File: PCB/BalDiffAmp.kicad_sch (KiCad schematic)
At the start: 15 parts, among them U5 TPA6120A2

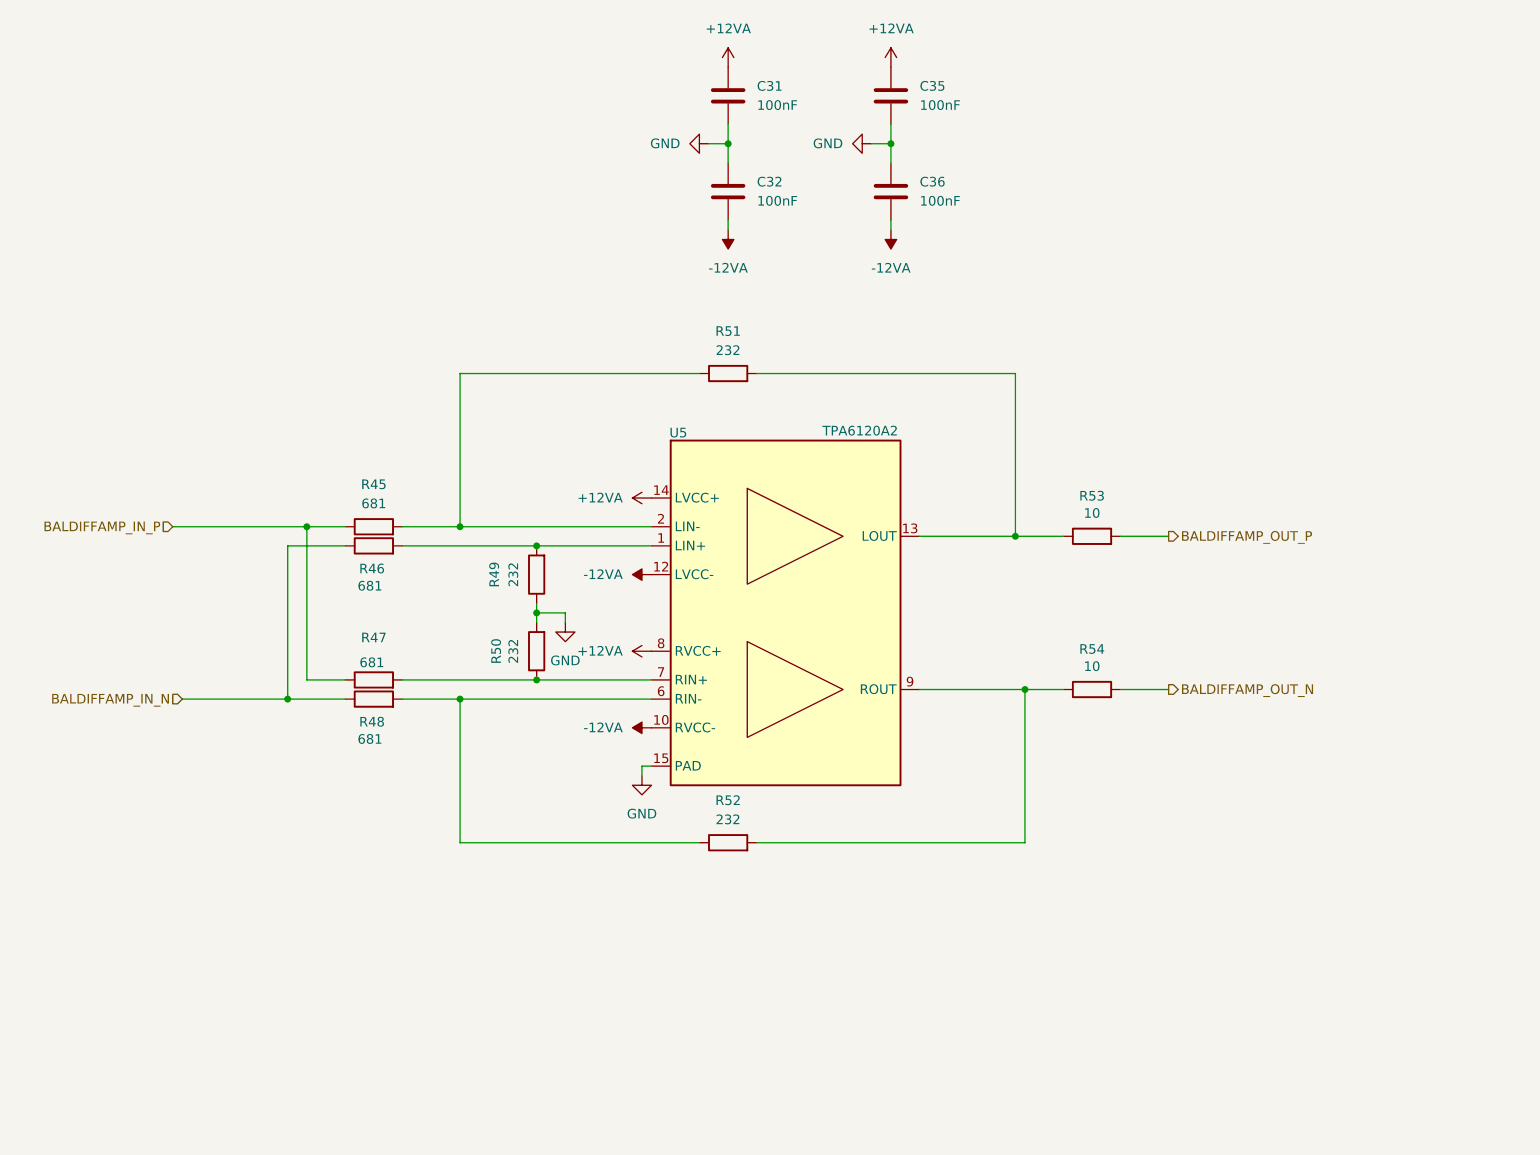
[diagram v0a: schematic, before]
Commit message: Added power supply and adjusted the AMP section to use only OPA1622 as output amp. In sync with Live 16
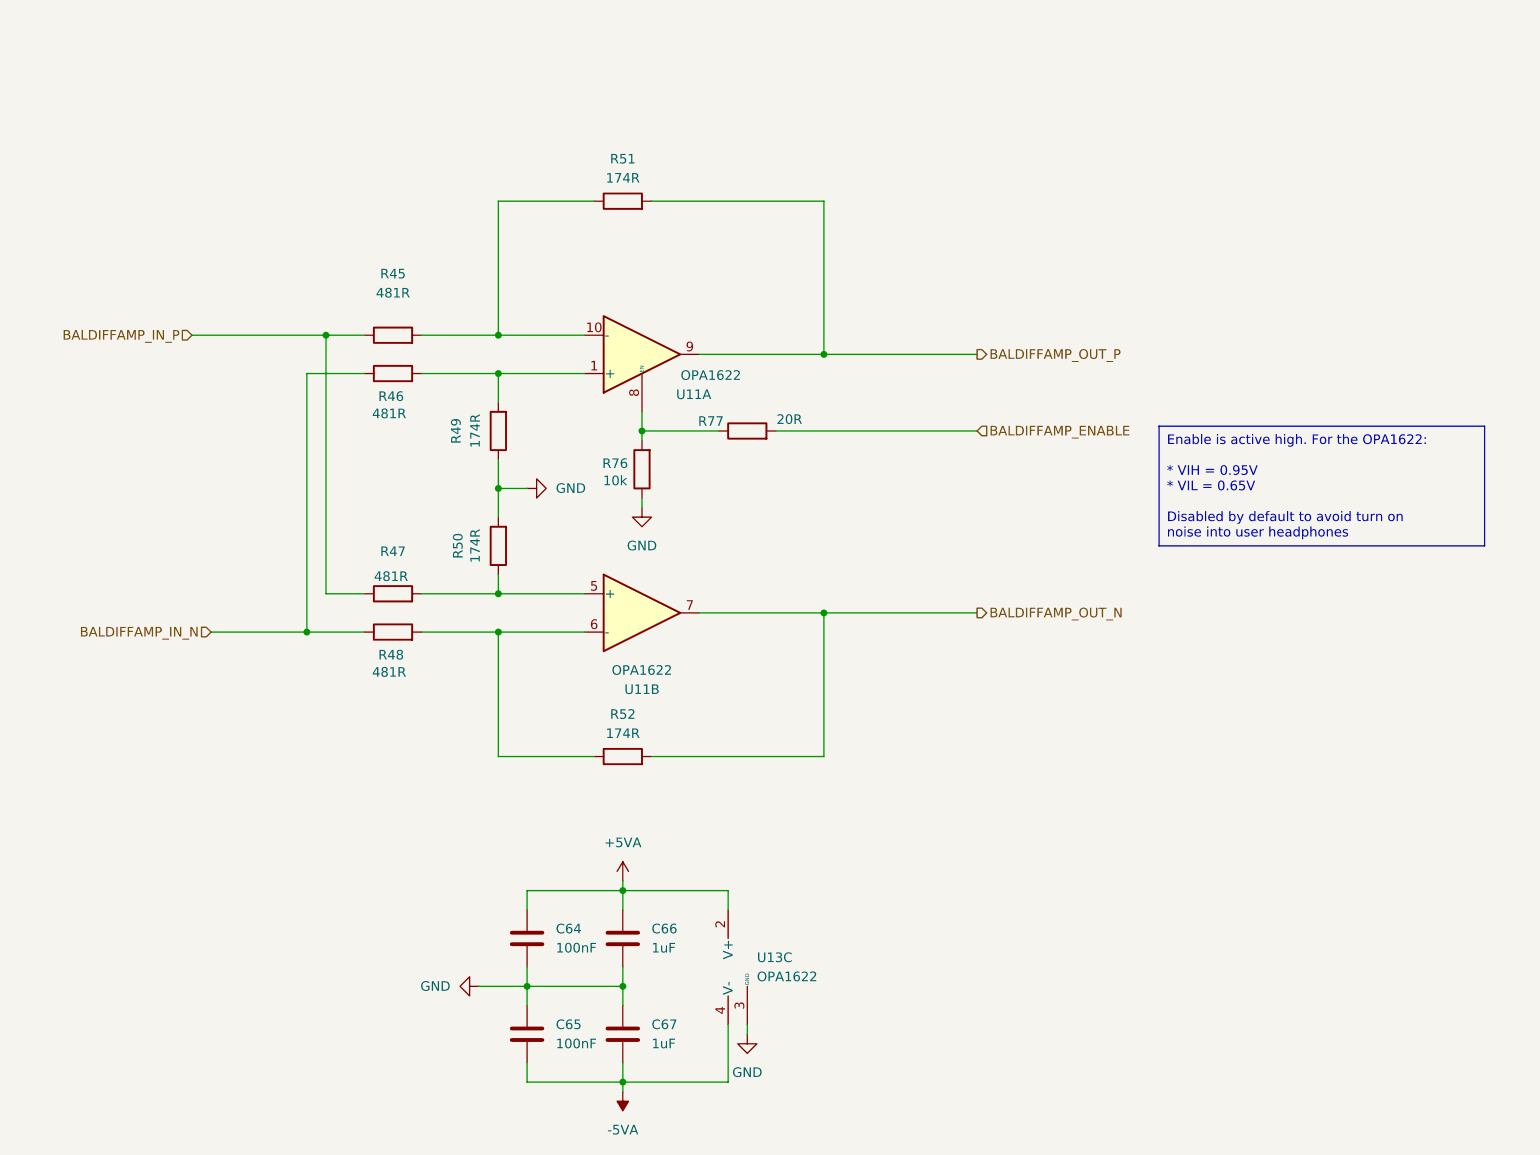
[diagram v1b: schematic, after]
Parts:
- removed C31, C32, C35, C36: 100nF, Capacitor_SMD:C_0402_1005Metric_Pad0.74x0.62mm_HandSolder, symbol Device:C
- removed R53, R54: 10, Resistor_SMD:R_0402_1005Metric_Pad0.72x0.64mm_HandSolder, symbol Device:R
- removed U5: TPA6120A2, _mahaudio KiCad Library:QFN-14_EP_3.5x3.5_Pitch0.5mm, symbol mahaudio_kicad_lib:TPA6120A2RGY
- added C64, C65: 100nF, Capacitor_SMD:C_0402_1005Metric_Pad0.74x0.62mm_HandSolder, symbol Device:C
- added C66, C67: 1uF, Capacitor_SMD:C_0402_1005Metric_Pad0.74x0.62mm_HandSolder, symbol Device:C
- added R76: 10k, Resistor_SMD:R_0402_1005Metric_Pad0.72x0.64mm_HandSolder, symbol Device:R
- added R77: 20R, Resistor_SMD:R_0402_1005Metric_Pad0.72x0.64mm_HandSolder, symbol Device:R
- added U11, U13: OPA1622, Package_SON:Texas_S-PVSON-N10, symbol Amplifier_Audio:OPA1622
- R45, R46, R47, R48: value 681 -> 481R; Tolerance (none) -> 0.1%
- R49, R50, R51, R52: value 232 -> 174R; Tolerance (none) -> 0.1%
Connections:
- net BALDIFFAMP_OUT_N: now also R52.2, U11.7
- net BALDIFFAMP_OUT_P: now also R51.2, U11.9
- net GND: now also C64.2, C65.1, C66.2, C67.1, R76.1, U13.3 (GND)
- net at R45.2, R51.1: now also U11.10 (-)
- net at R46.2, R49.2: now also U11.1 (+)
- net at R48.2, R52.1: now also U11.6 (-)
- net at R47.2, R50.1: now also U11.5 (+)
- new net: R76.2, R77.1, U11.8 (EN)
- new net +5VA: C64.1, C66.1, U13.2 (V+)
- new net -5VA: C65.2, C67.2, U13.11 (V-), U13.4 (V-)
- new net BALDIFFAMP_ENABLE: R77.2
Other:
- moved on the sheet: R45, R46, R47, R48, R49, R50, R51, R52

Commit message: Added E2P and testpoints
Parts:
- C66, C67: footprint Capacitor_SMD:C_0402_1005Metric_Pad0.74x0.62mm_HandSolder -> Capacitor_SMD:C_0603_1608Metric_Pad1.08x0.95mm_HandSolder
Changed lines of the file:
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@@
 			)
 		)
-		(property "Footprint" "Capacitor_SMD:C_0402_1005Metric_Pad0.74x0.62mm_HandSolder"
+		(property "Footprint" "Capacitor_SMD:C_0603_1608Metric_Pad1.08x0.95mm_HandSolder"
 			(at 140.6652 153.67 0)
 			(effects
@@
 			)
 		)
-		(property "Footprint" "Capacitor_SMD:C_0402_1005Metric_Pad0.74x0.62mm_HandSolder"
+		(property "Footprint" "Capacitor_SMD:C_0603_1608Metric_Pad1.08x0.95mm_HandSolder"
 			(at 140.6652 166.37 0)
 			(effects

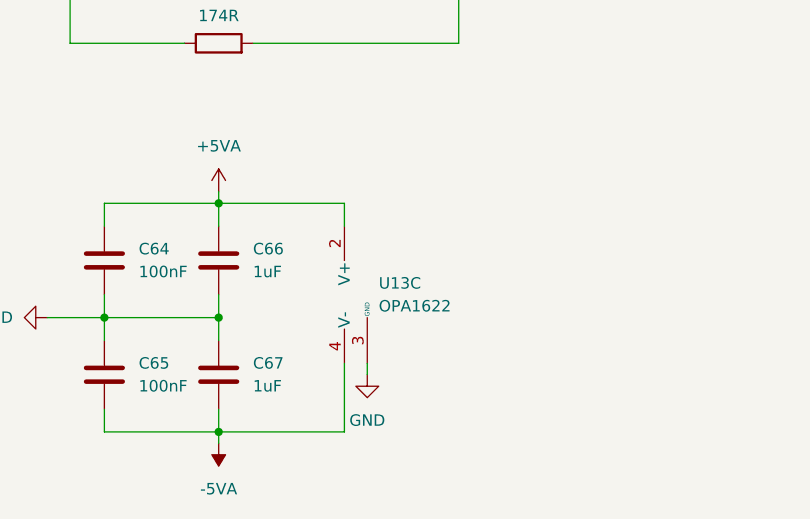
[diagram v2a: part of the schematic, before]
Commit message: Finished basic placement
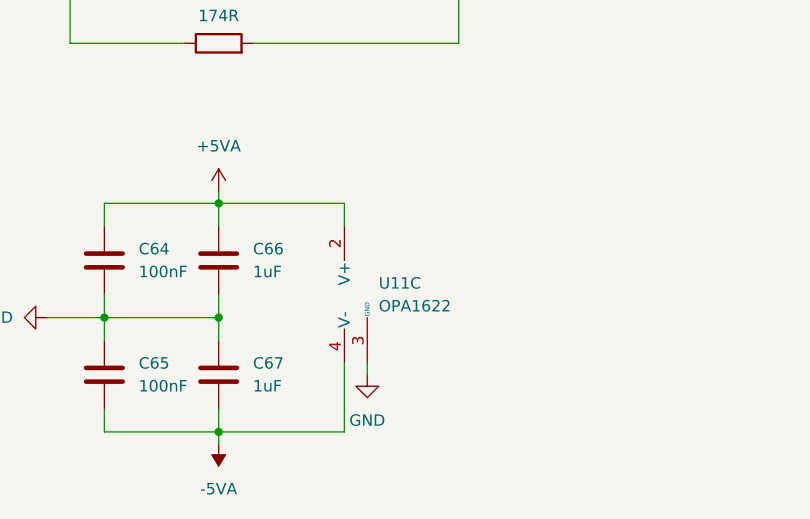
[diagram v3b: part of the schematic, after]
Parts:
- renumbered U13 to U11
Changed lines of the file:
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@@
 		(dnp no)
 		(fields_autoplaced yes)
-		(property "Reference" "U13"
+		(property "Reference" "U11"
 			(at 157.48 152.3999 0)
 			(effects
@@
 			(project "mhd314"
 				(path "/afee45fc-2361-4efb-9cde-757fc2efd57b/913309c3-489c-42b3-afc6-179d92cffcea/1a7c2388-0e9a-4978-b565-aab0f7919656"
-					(reference "U13")
+					(reference "U11")
 					(unit 3)
 				)
 				(path "/afee45fc-2361-4efb-9cde-757fc2efd57b/913309c3-489c-42b3-afc6-179d92cffcea/9f9c7045-f919-4646-b118-b603b053c849"
-					(reference "U12")
+					(reference "U4")
 					(unit 3)
 				)

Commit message: Routing revised, added some missing parameters to components
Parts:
- C66, C67: Voltage 6.3V -> 16V
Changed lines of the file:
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@@
 			)
 		)
-		(property "Voltage" "6.3V"
+		(property "Voltage" "16V"
 			(at 139.7 149.86 0)
 			(effects
@@
 			)
 		)
-		(property "Voltage" "6.3V"
+		(property "Voltage" "16V"
 			(at 139.7 162.56 0)
 			(effects

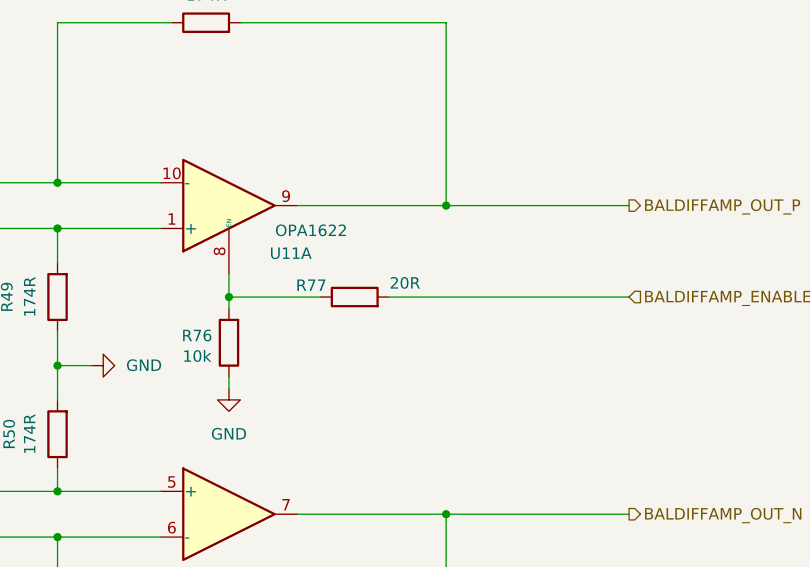
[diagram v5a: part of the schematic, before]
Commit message: Updated PCB with digital traxce suggestions. Added JLCPCB Pns
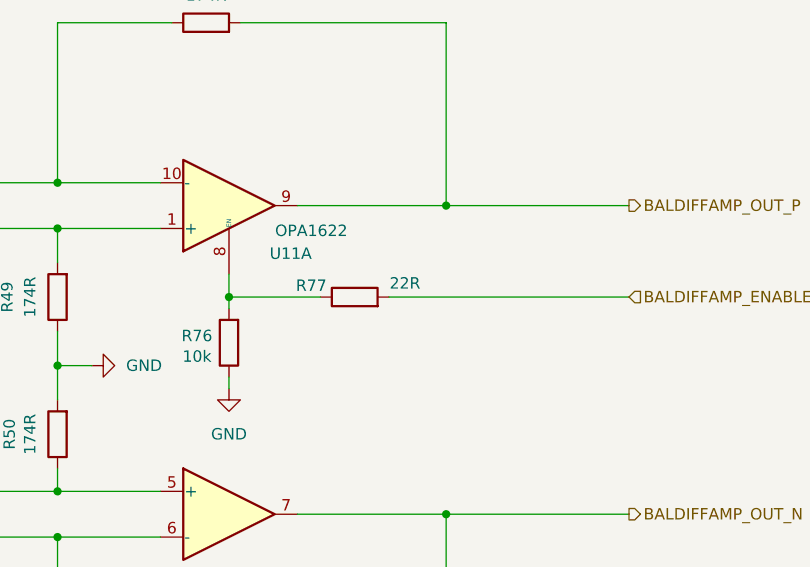
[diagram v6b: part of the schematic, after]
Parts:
- C64, C65: JLCPCBPn (none) -> C1525; Voltage 25V -> 16V
- C66, C67: JLCPCBPn (none) -> C15849
- R76: JLCPCBPn (none) -> C25744
- R77: value 20R -> 22R; JLCPCBPn (none) -> C25092
- U11: JLCPCBPn (none) -> C2876559
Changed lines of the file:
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@@
 			)
 		)
-		(property "Voltage" "25V"
+		(property "Voltage" "16V"
+			(at 127 149.86 0)
+			(effects
+				(font
+					(size 1.27 1.27)
+				)
+				(hide yes)
+			)
+		)
+		(property "JLCPCBPn" "C1525"
 			(at 127 149.86 0)
 			(effects
@@
 			)
 		)
+		(property "JLCPCBPn" "C2876559"
+			(at 142.24 106.68 0)
+			(effects
+				(font
+					(size 1.27 1.27)
+				)
+				(hide yes)
+			)
+		)
 		(pin "4"
 		)
@@
 			)
 		)
+		(property "JLCPCBPn" "C15849"
+			(at 139.7 149.86 0)
+			(effects
+				(font
+					(size 1.27 1.27)
+				)
+				(hide yes)
+			)
+		)
 		(pin "1"
 		)
@@
 			)
 		)
+		(property "JLCPCBPn" "C2876559"
+			(at 156.21 153.67 0)
+			(effects
+				(font
+					(size 1.27 1.27)
+				)
+				(hide yes)
+			)
+		)
 		(pin "4"
 		)
@@
 			)
 		)
-		(property "Voltage" "25V"
+		(property "Voltage" "16V"
+			(at 127 162.56 0)
+			(effects
+				(font
+					(size 1.27 1.27)
+				)
+				(hide yes)
+			)
+		)
+		(property "JLCPCBPn" "C1525"
 			(at 127 162.56 0)
 			(effects
@@
 			)
 		)
+		(property "JLCPCBPn" "C2876559"
+			(at 142.24 72.39 0)
+			(effects
+				(font
+					(size 1.27 1.27)
+				)
+				(hide yes)
+			)
+		)
 		(pin "4"
 		)
@@
 		)
 		(property "Tolerance" "5%"
+			(at 142.24 87.63 0)
+			(effects
+				(font
+					(size 1.27 1.27)
+				)
+				(hide yes)
+			)
+		)
+		(property "JLCPCBPn" "C25744"
 			(at 142.24 87.63 0)
 			(effects
@@
 			)
 		)
-		(property "Value" "20R"
+		(property "Value" "22R"
 			(at 161.798 81.026 90)
 			(effects
@@
 		(property "Tolerance" "5%"
 			(at 156.21 82.55 90)
+			(effects
+				(font
+					(size 1.27 1.27)
+				)
+				(hide yes)
+			)
+		)
+		(property "JLCPCBPn" "C25092"
+			(at 156.21 82.55 0)
 			(effects
 				(font
@@
 			(at 139.7 162.56 0)
 			(effects
+				(font
+					(size 1.27 1.27)
+				)
+				(hide yes)
+			)
+		)
+		(property "JLCPCBPn" "C15849"
+			(at 139.7 162.56 0)
+			(effects

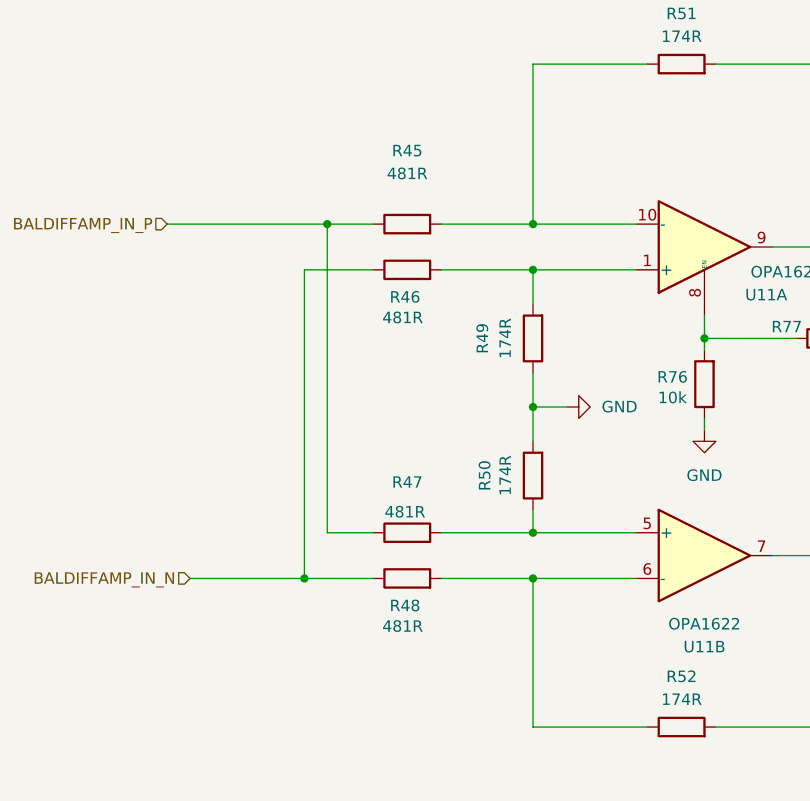
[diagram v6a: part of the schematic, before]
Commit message: Changed resistor values to match JLCPCB + general board revision
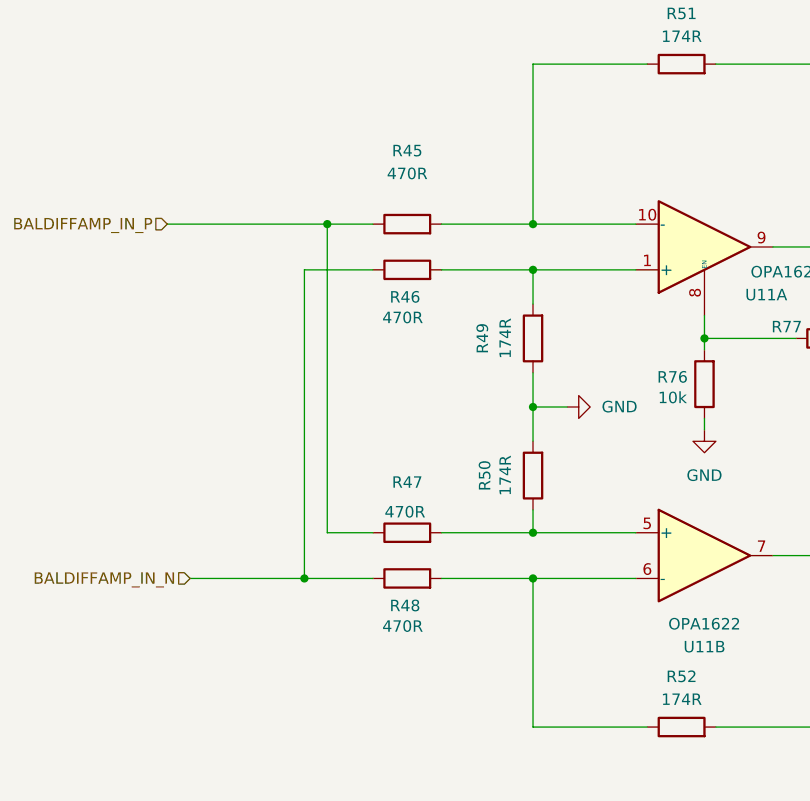
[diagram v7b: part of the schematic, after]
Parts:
- R45, R46, R47, R48: value 481R -> 470R; JLCPCBPn (none) -> C445590
- R49, R50, R51, R52: JLCPCBPn (none) -> C852566
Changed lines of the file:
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@@
+			)
+		)
+		(property "JLCPCBPn" "C852566"
+			(at 139.7 52.07 0)
+			(effects
+				(font
+					(size 1.27 1.27)
+				)
+				(hide yes)
 			)
 		)
@@
 			)
 		)
-		(property "Value" "481R"
+		(property "Value" "470R"
 			(at 108.712 80.264 90)
 			(effects
@@
 		)
 		(property "Tolerance" "0.1%"
+			(at 109.22 74.93 0)
+			(effects
+				(font
+					(size 1.27 1.27)
+				)
+				(hide yes)
+			)
+		)
+		(property "JLCPCBPn" "C445590"
 			(at 109.22 74.93 0)
 			(effects
@@
 			)
 		)
-		(property "Value" "481R"
+		(property "Value" "470R"
 			(at 108.712 114.554 90)
 			(effects
@@
 		)
 		(property "Tolerance" "0.1%"
+			(at 109.22 109.22 0)
+			(effects
+				(font
+					(size 1.27 1.27)
+				)
+				(hide yes)
+			)
+		)
+		(property "JLCPCBPn" "C445590"
 			(at 109.22 109.22 0)
 			(effects
@@
 		)
 		(property "Tolerance" "0.1%"
+			(at 123.19 97.79 0)
+			(effects
+				(font
+					(size 1.27 1.27)
+				)
+				(hide yes)
+			)
+		)
+		(property "JLCPCBPn" "C852566"
 			(at 123.19 97.79 0)
 			(effects
@@
 			)
 		)
-		(property "Value" "481R"
+		(property "Value" "470R"
 			(at 108.966 101.854 90)
 			(effects
@@
 		)
 		(property "Tolerance" "0.1%"
+			(at 109.22 104.14 0)
+			(effects
+				(font
+					(size 1.27 1.27)
+				)
+				(hide yes)
+			)
+		)
+		(property "JLCPCBPn" "C445590"
 			(at 109.22 104.14 0)
 			(effects
@@
 			)
 		)
-		(property "Value" "481R"
+		(property "Value" "470R"
 			(at 109.22 64.262 90)
 			(effects
@@
 		)
 		(property "Tolerance" "0.1%"
+			(at 109.22 69.85 0)
+			(effects
+				(font
+					(size 1.27 1.27)
+				)
+				(hide yes)
+			)
+		)
+		(property "JLCPCBPn" "C445590"
 			(at 109.22 69.85 0)
 			(effects
@@
 			)
 		)
+		(property "JLCPCBPn" "C852566"
+			(at 139.7 125.73 0)
+			(effects
+				(font
+					(size 1.27 1.27)
+				)
+				(hide yes)
+			)
+		)
 		(pin "1"
 		)
@@
 			(at 123.19 82.55 0)
 			(effects
+				(font
+					(size 1.27 1.27)
+				)
+				(hide yes)
+			)
+		)
+		(property "JLCPCBPn" "C852566"
+			(at 123.19 82.55 0)
+			(effects
